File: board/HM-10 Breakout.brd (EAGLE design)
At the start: 24 x 36.6 mm, 21 parts, among them U1 V_REG_LDOSMD

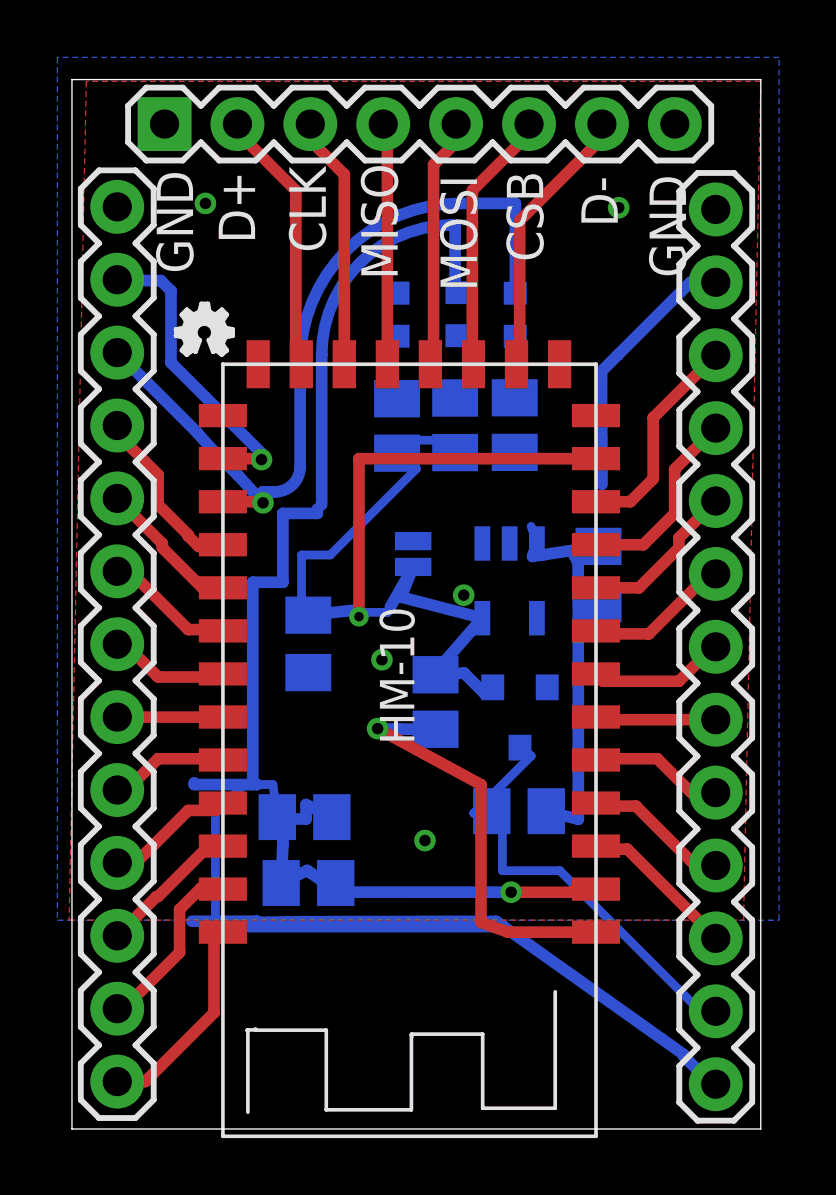
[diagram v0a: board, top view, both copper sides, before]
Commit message: Overhaul PCB
Cleanup typography on silkscreen
Remove no connection lines
Replace HM-10 Eagle part with a more faithful version
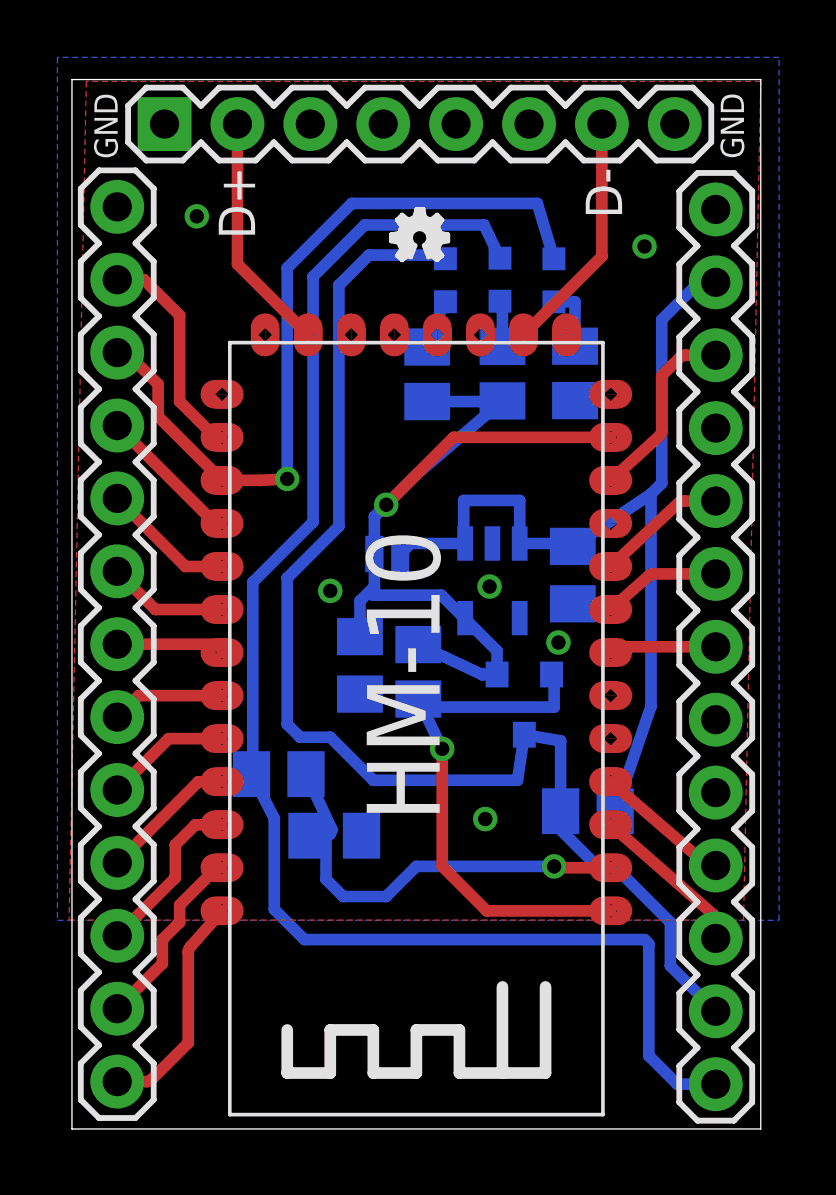
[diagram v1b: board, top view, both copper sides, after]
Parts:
- removed U$1: BLE-HM-10, Random parts:BLE-HM-10
- removed U$2: (no value), ohw-logo:OSHW_FILLX350_NOTEXT
- added U2: HM-10, HM-10_BLE:HM-10
- moved U$3 8.19 mm to (11.1, 30.3)
- moved R7 2.77 mm to (17.5, 26.3)
- moved R2 2.44 mm to (15.0, 26.3)
- moved R5 2.40 mm to (18.0, 11.1)
- moved R1 2.08 mm to (12.4, 26.3)
- moved TX_LED 2.04 mm to (13.0, 29.6)
- moved C2 1.95 mm to (10.0, 16.2)
- moved RX_LED 1.92 mm to (14.9, 29.6)
- moved R4 1.88 mm to (9.14, 10.2)
- moved CONN_LED 1.81 mm to (16.8, 29.6)
- moved R3 1.75 mm to (7.20, 12.4)
- moved R6 1.21 mm to (12.1, 15.9)
- moved C1 0.90 mm to (17.4, 19.3)
- moved SJ1 0.90 mm to (11.0, 20.0), turned to 180 degrees
- moved U1 0.60 mm to (14.7, 19.1)
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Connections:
- removed net N$25: JP2.12, U$1.PIO0
- removed net N$28: JP3.2, U$1.USB_D+
- removed net N$29: JP3.3, U$1.SPI_CLK
- removed net N$30: JP3.4, U$1.SPI_MISO
- removed net N$31: JP3.5, U$1.SPI_MOSI
- removed net N$32: JP3.6, U$1.SPI_CSB
- removed net N$33: JP3.7, U$1.USB_D-
- net 3_3V: now also U2.12; no longer U$1.3.3V
- net GND: now also U2.13, U2.14, U2.21, U2.22; no longer U$1.GND1, U$1.GND2, U$1.GND3, U$1.GND4
- net HVTX->LVRX: now also U2.2; no longer U$1.UART_RX
- net LVRX->HVTX: now also U2.1; no longer U$1.UART_TX
- net N$10: now also U2.4; no longer U$1.UART_RTS
- net N$11: now also U2.3; no longer U$1.UART_CTS
- net N$14: now also JP2.9, U2.26; no longer JP2.1, U$1.PIO11
- net N$15: now also JP2.8, U2.27; no longer JP2.2, U$1.PIO10
- net N$16: now also JP2.7, U2.28; no longer JP2.3, U$1.PIO9
- net N$17: now also JP2.6, U2.29; no longer JP2.4, U$1.PIO8
- net N$18: now also U2.30; no longer U$1.PIO7
- net N$19: now also JP2.4, U2.31; no longer JP2.6, U$1.PIO6
- net N$2: now also U2.24; no longer U$1.PIO1
- net N$20: now also JP2.3, U2.32; no longer JP2.7, U$1.PIO5
- net N$21: now also JP2.2, U2.33; no longer JP2.8, U$1.PIO4
- net N$22: now also JP2.1, U2.34; no longer JP2.9, U$1.PIO3
- net N$23: now also JP2.12, U2.23; no longer JP2.10, U$1.PIO2
- net N$3: now also U2.11; no longer U$1.RESET
- net N$4: now also JP3.7, U2.15; no longer JP1.4, U$1.AIO1
- net N$5: now also JP1.7, U2.7; no longer JP1.5, U$1.AIO0
- net N$6: now also JP1.5, U2.9; no longer JP1.6, U$1.PCM_SYNC
- net N$7: now also JP1.6, U2.8; no longer JP1.7, U$1.PCM_IN
- net N$8: now also JP2.10, U2.25; no longer JP1.8, U$1.PCM_OUT
- net N$9: now also JP3.2, U2.20; no longer JP1.9, U$1.PCM_CLK
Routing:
- net TX: track 15.8 -> 44.0 mm
- net RX: track 66.2 -> 51.3 mm
- net N$25: track 10.6 -> 0.00 mm, vias 1 -> 0
- net N$33: track 9.60 -> 0.00 mm
- net N$28: track 9.29 -> 0.00 mm
- net N$32: track 9.20 -> 0.00 mm
- net N$29: track 8.86 -> 0.00 mm
- net N$31: track 8.74 -> 0.00 mm
- net 5V: track 24.0 -> 32.5 mm
- net N$30: track 8.43 -> 0.00 mm
- net 3_3V: track 38.9 -> 31.8 mm
- net N$9: track 4.68 -> 8.37 mm
- net LVRX->HVTX: track 15.0 -> 18.6 mm
- net N$22: track 5.06 -> 8.05 mm
- net N$14: track 7.30 -> 4.63 mm
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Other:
- board text added: "0"
- board text added: "1"
- board text added: "10"
- board text added: "11"
- board text added: "2"
- board text added: "3"
- board text added: "4"
- board text added: "5"
- board text added: "6"
- board text added: "7"
- board text added: "8"
- board text added: "9"
- board text added: "DBGC"
- board text added: "DBGD"
- board text added: "P2_0"
- board text removed: "AIO0"
- board text removed: "AIO1"
- board text removed: "CLK"
- board text removed: "CSB"
- board text removed: "HM-10"
- board text removed: "IO0"
- board text removed: "IO1"
- board text removed: "IO10"
- board text removed: "IO11"
- board text removed: "IO2"
- board text removed: "IO3"
- board text removed: "IO4"
- board text removed: "IO5"
- board text removed: "IO6"
- board text removed: "IO7"
- board text removed: "IO8"
- board text removed: "IO9"
- board text removed: "MISO"
- board text removed: "MOSI"
- board text removed: "PCLK"
- board text removed: "PIN"
- board text removed: "POUT"
- board text removed: "PSYNC"

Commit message: Shrink board
Remove top row of pins
Change silkscreen to note change to SPI over USB
Add version number and text to silkscreen
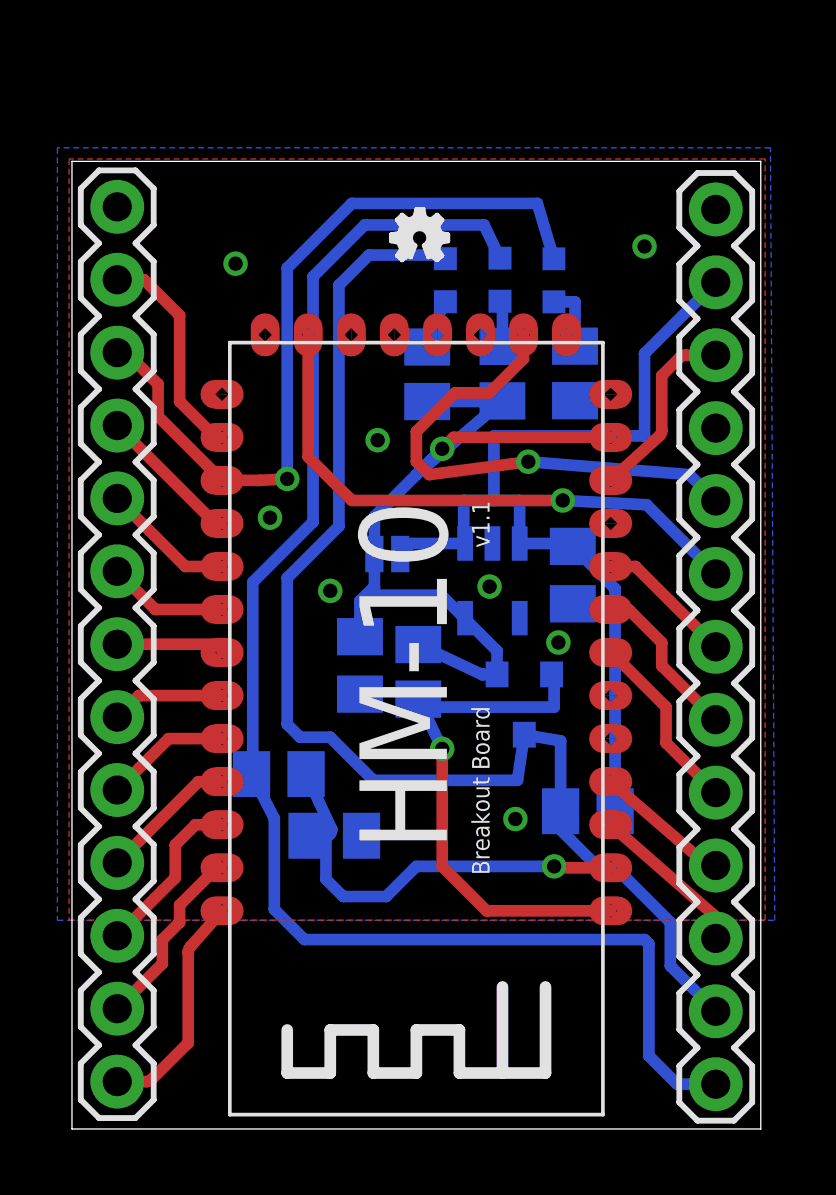
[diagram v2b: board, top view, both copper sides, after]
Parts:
- removed JP3: (no value), SparkFun:1X08
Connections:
- net GND: no longer JP3.1, JP3.8
- net N$4: now also JP1.5; no longer JP3.7
- net N$5: now also JP1.9; no longer JP1.7
- net N$6: now also JP1.8, U2.8; no longer JP1.5, U2.9
- net N$7: now also JP1.7, U2.9; no longer JP1.6, U2.8
- net N$9: now also JP1.6; no longer JP3.2
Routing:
- net N$9: track 8.37 -> 20.2 mm, vias 0 -> 1
- net N$4: track 8.48 -> 17.7 mm, vias 0 -> 1
- net N$5: track 3.71 -> 6.41 mm
- net N$6: track 4.55 -> 5.73 mm
- net 5V: track 32.5 -> 33.6 mm
- net N$7: track 4.12 -> 4.82 mm
- net GND: vias 6 -> 8
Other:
- board size 24 x 36.6 mm -> 24 x 33.7 mm
- board text added: "Breakout Board"
- board text added: "CON"
- board text added: "SCL"
- board text added: "SDA"
- board text added: "v1.1"
- board text removed: "CONN"
- board text removed: "D+"
- board text removed: "D-"

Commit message: Shift components toward center on bottom layer
Make pin description text larger
Switch from DBGD to DD notation
Rotate LED labels 45 degrees
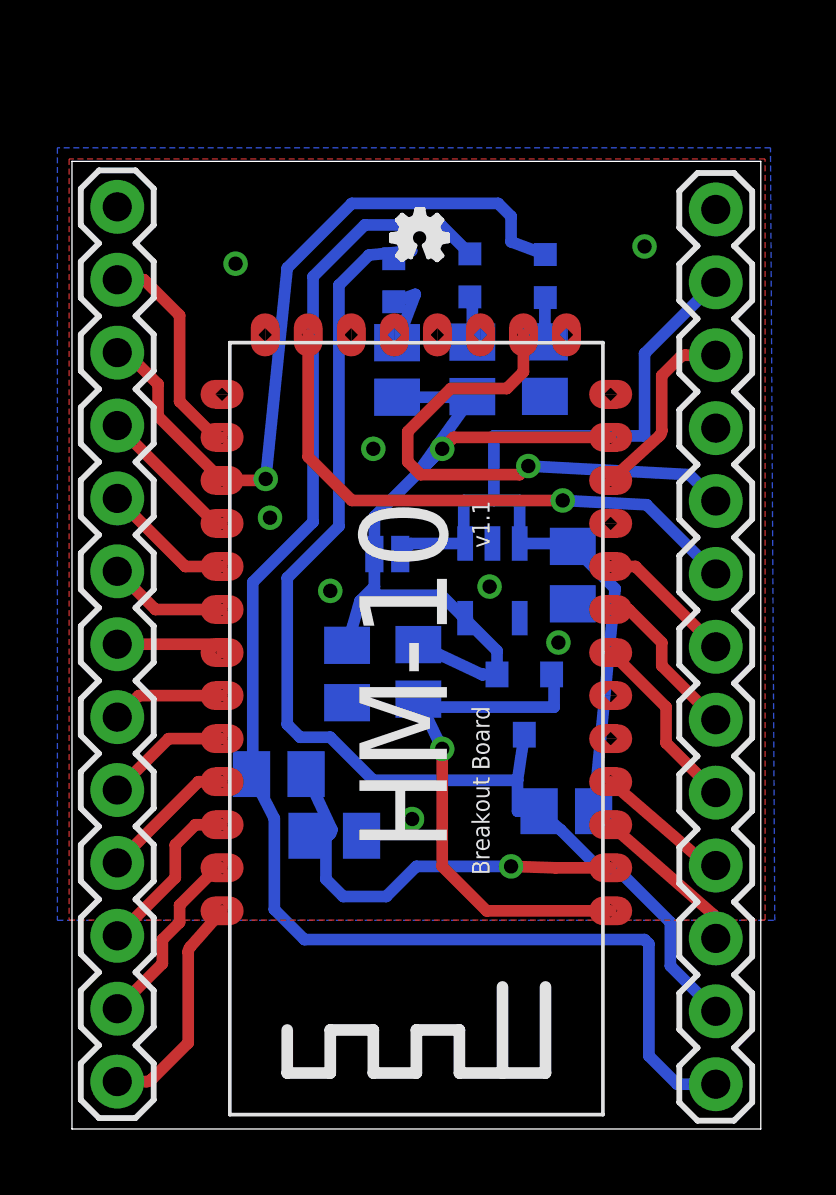
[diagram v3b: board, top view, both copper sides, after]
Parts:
- moved TX_LED 1.80 mm to (11.2, 29.6)
- moved R7 1.06 mm to (16.5, 26.5)
- moved R1 1.06 mm to (11.3, 26.4)
- moved R2 1.06 mm to (13.9, 26.5)
- moved RX_LED 1.06 mm to (13.9, 29.7)
- moved R5 0.75 mm to (17.2, 11.1)
- moved C2 0.54 mm to (9.58, 15.9)
- moved CONN_LED 0.34 mm to (16.5, 29.7)
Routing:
- net TX: track 44.0 -> 41.9 mm
- net RX: track 51.3 -> 49.9 mm
- net N$2: track 27.4 -> 26.1 mm
- net N$4: track 17.7 -> 18.7 mm
- net N$26: track 2.28 -> 1.56 mm
- net N$24: track 1.91 -> 2.59 mm
- net GND: track 0.53 -> 0.00 mm
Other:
- board text added: "DC"
- board text added: "DD"
- board text removed: "DBGC"
- board text removed: "DBGD"

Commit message: Tented vias
Cleaned up routes more
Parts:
- moved R5 1.54 mm to (15.9, 11.8)
- moved TX_LED 0.21 mm to (11.4, 29.7)
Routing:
- net 3_3V: track 31.3 -> 30.4 mm
- net N$24: track 2.59 -> 1.70 mm
- net HVTX->LVRX: track 15.8 -> 14.9 mm

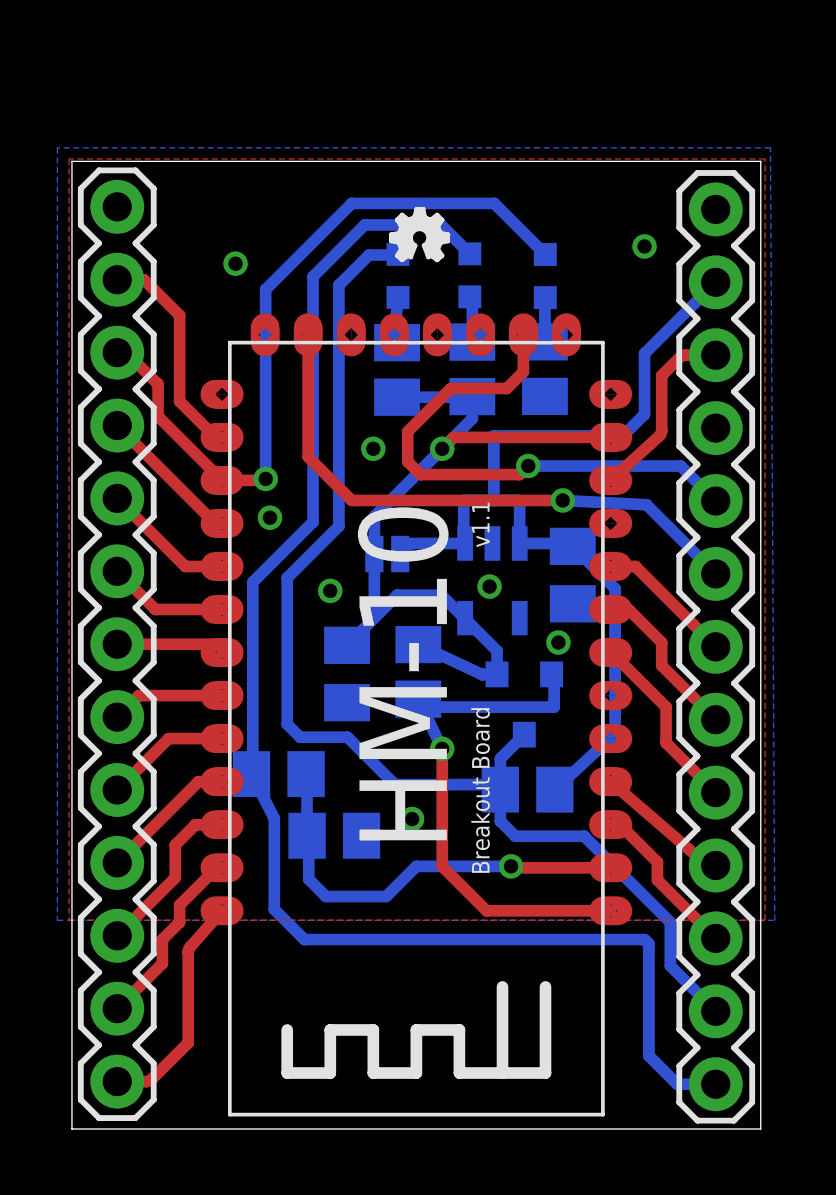
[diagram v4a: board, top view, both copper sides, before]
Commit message: Update images
Rotate LEDs 45 degrees
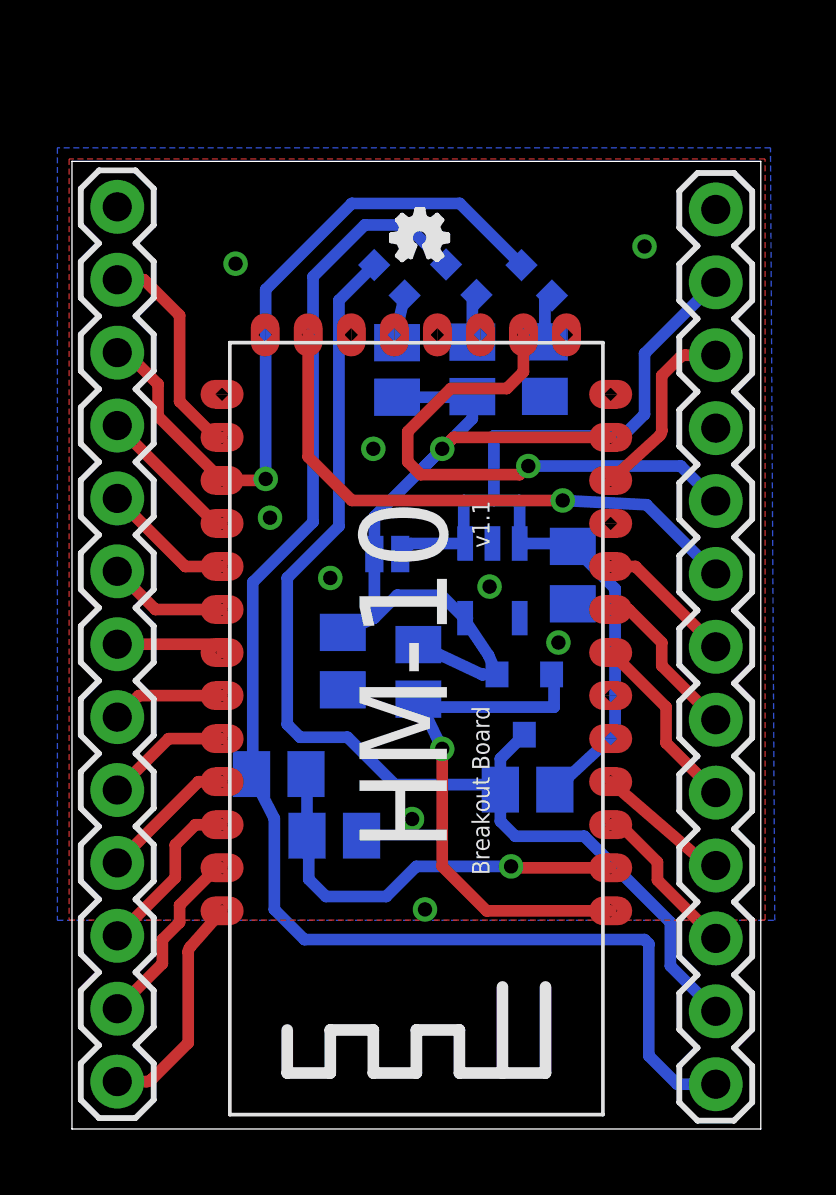
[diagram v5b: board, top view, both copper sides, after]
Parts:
- moved C2 0.47 mm to (9.43, 16.3)
- moved CONN_LED 0.34 mm to (16.2, 29.6), turned to 135 degrees
- moved RX_LED 0.34 mm to (13.6, 29.6), turned to 315 degrees
- moved TX_LED 0.34 mm to (11.1, 29.6), turned to 315 degrees
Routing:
- net TX: track 41.4 -> 40.1 mm
- net RX: track 49.9 -> 49.3 mm
- net N$2: track 26.0 -> 25.3 mm
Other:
- board text added: "CONN"
- board text removed: "CON"

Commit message: Add OSHW logos back
Add attribution text to bottom layer
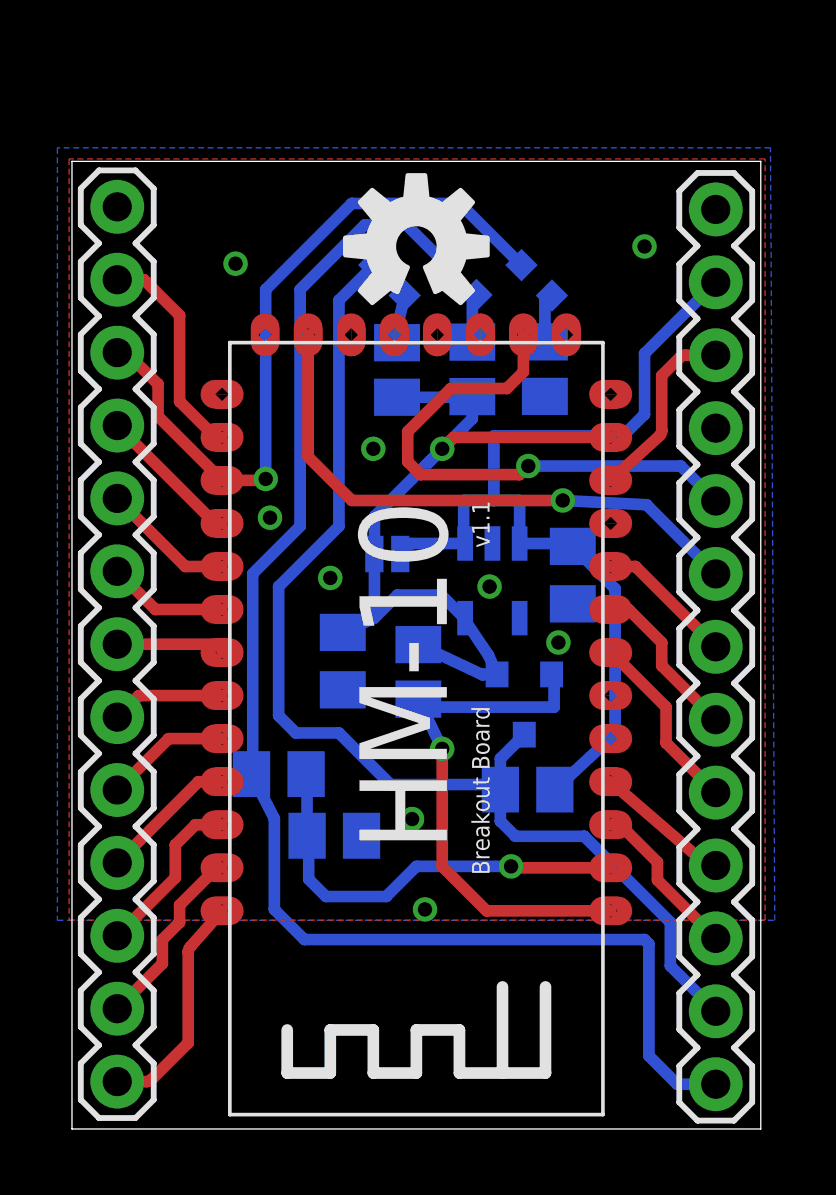
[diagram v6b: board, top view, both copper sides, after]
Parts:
- removed U$3: (no value), ohw-logo:OSHW_FILLX70_NOTEXT
- added U$1: (no value), SparkFun-Aesthetics:OSHW-LOGO-S
- added U$2: (no value), SparkFun-Aesthetics:OSHW-LOGO-M
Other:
- board text added: "HM-10 Breakout"
- board text added: "Nick Walker"
